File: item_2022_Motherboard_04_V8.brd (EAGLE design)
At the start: 160 x 100 mm, 130 parts, among them IC1 MCP602SN, IC2 LD117AS33TR, IC3 MCP1525TO, IC4 MCP6S26, IC5 MCP6004SO, IC6 MCP6004SO, IC7 MCP3204SL, IC8 LM336LP, IC9 MCP6004SO, U1 ESP32-DEVKITC-32D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

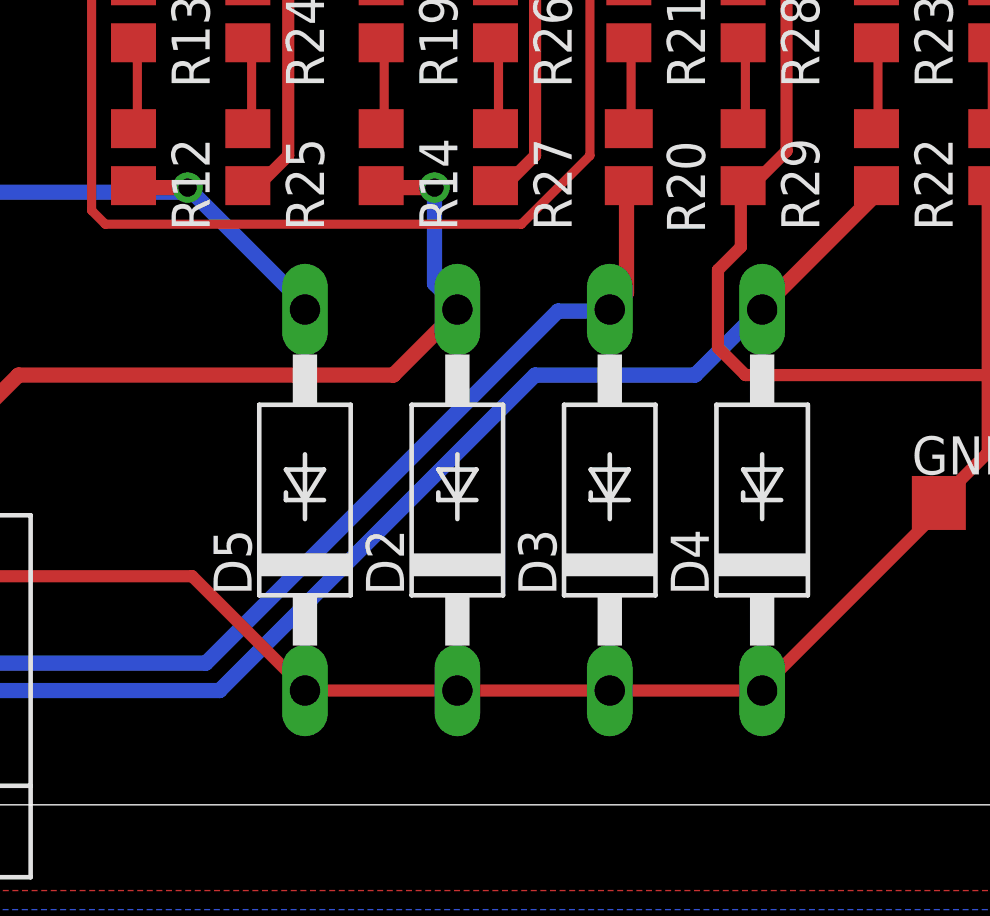
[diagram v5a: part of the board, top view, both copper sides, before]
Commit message: spostati BZW su Frontend da motherboard
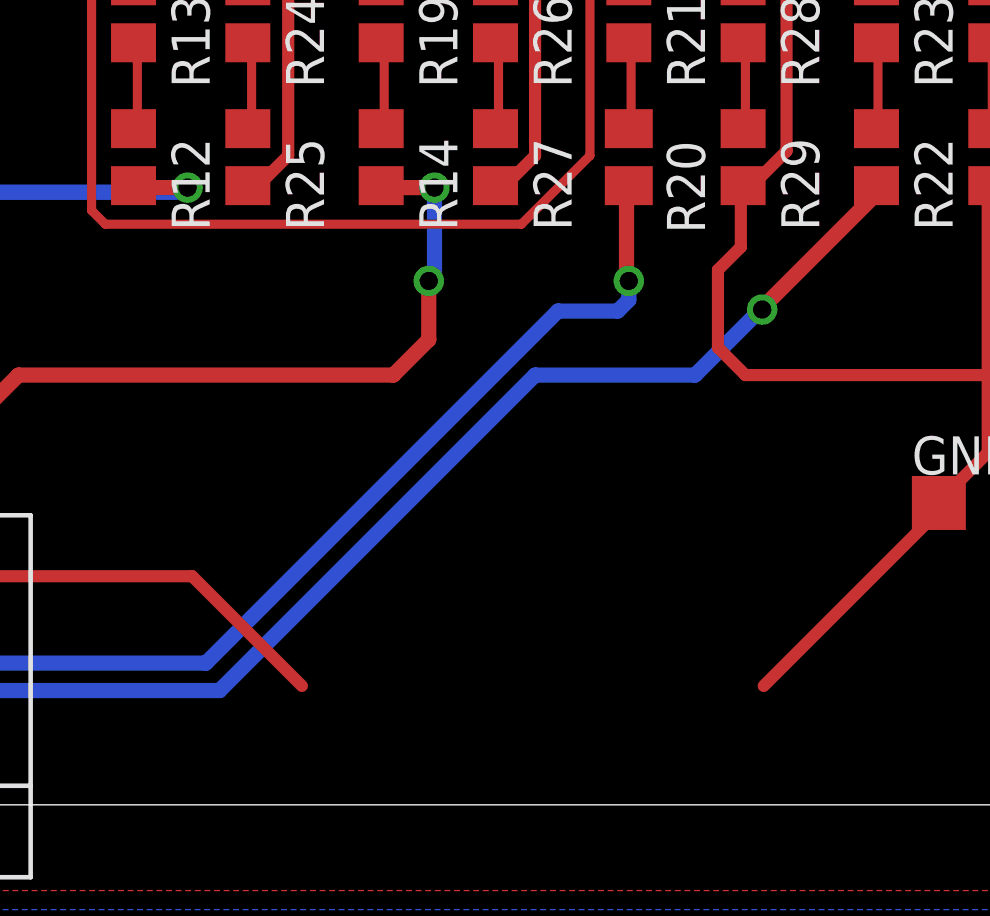
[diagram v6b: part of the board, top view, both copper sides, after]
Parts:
- removed D2, D3, D4, D5: BZW06-10B, diode_LargePads:F126Z12
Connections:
- net GND: no longer D2.C, D3.C, D4.C, D5.C
- net SPEED1+: no longer D3.A
- net SPEED2+: no longer D4.A
- net TORQUE1+: no longer D5.A
- net TORQUE2+: no longer D2.A
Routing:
- net GND: track 943.0 -> 927.4 mm
- net TORQUE1+: track 95.4 -> 89.6 mm
- net TORQUE2+: track 107.3 -> 106.9 mm, vias 1 -> 2
- net SPEED1+: track 111.4 -> 111.7 mm, vias 0 -> 1
- net SPEED2+: vias 0 -> 1
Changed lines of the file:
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@@
 <setting verticaltext="up"/>
 </settings>
-<grid distance="0.0125" unitdist="inch" unit="mm" style="lines" multiple="2" display="yes" altdistance="0.025" altunitdist="inch" altunit="inch"/>
+<grid distance="0.0125" unitdist="inch" unit="mil" style="lines" multiple="2" display="yes" altdistance="0.025" altunitdist="inch" altunit="inch"/>
 <layers>
 <layer number="1" name="Top" color="4" fill="1" visible="yes" active="yes"/>
@@
 <attribute name="VALUE" x="151.765" y="56.515" size="1.27" layer="27" rot="R270"/>
 </element>
-<element name="D2" library="diode_LargePads" package="F126Z12" value="BZW06-10B" x="133.35" y="10.16" smashed="yes" rot="R90">
-<attribute name="NAME" x="131.572" y="6.985" size="1.27" layer="25" ratio="10" rot="R90"/>
-<attribute name="POPULARITY" value="0" x="441.95" y="10.16" size="1.778" layer="27" rot="R90" display="off"/>
-<attribute name="VALUE" x="136.398" y="6.985" size="1.27" layer="27" ratio="10" rot="R90"/>
-</element>
-<element name="D3" library="diode_LargePads" package="F126Z12" value="BZW06-10B" x="138.43" y="10.16" smashed="yes" rot="R90">
-<attribute name="NAME" x="136.652" y="6.985" size="1.27" layer="25" ratio="10" rot="R90"/>
-<attribute name="POPULARITY" value="0" x="462.33" y="-17.84" size="1.778" layer="27" rot="R90" display="off"/>
-<attribute name="VALUE" x="141.478" y="6.985" size="1.27" layer="27" ratio="10" rot="R90"/>
-</element>
-<element name="D4" library="diode_LargePads" package="F126Z12" value="BZW06-10B" x="143.51" y="10.16" smashed="yes" rot="R90">
-<attribute name="NAME" x="141.732" y="6.985" size="1.27" layer="25" ratio="10" rot="R90"/>
-<attribute name="POPULARITY" value="0" x="467.41" y="10.16" size="1.778" layer="27" rot="R90" display="off"/>
-<attribute name="VALUE" x="146.558" y="6.985" size="1.27" layer="27" ratio="10" rot="R90"/>
-</element>
-<element name="D5" library="diode_LargePads" package="F126Z12" value="BZW06-10B" x="128.27" y="10.16" smashed="yes" rot="R90">
-<attribute name="NAME" x="126.492" y="6.985" size="1.27" layer="25" ratio="10" rot="R90"/>
-<attribute name="POPULARITY" value="0" x="467.47" y="-17.84" size="1.778" layer="27" rot="R90" display="off"/>
-<attribute name="VALUE" x="131.318" y="6.985" size="1.27" layer="27" ratio="10" rot="R90"/>
-</element>
 <element name="IC7" library="MCP3204_MCP3208" package="SO14" value="MCP3204SL" x="151.765" y="67.31" smashed="yes">
 <attribute name="NAME" x="146.939" y="65.405" size="1.27" layer="25" ratio="10" rot="R90"/>
@@
 <contactref element="R11" pad="1"/>
 <contactref element="C15" pad="2"/>
-<contactref element="D4" pad="C"/>
-<contactref element="D3" pad="C"/>
-<contactref element="D2" pad="C"/>
-<contactref element="D5" pad="C"/>
 <contactref element="R25" pad="2"/>
 <contactref element="C16" pad="2"/>
@@
 <wire x1="79.0956" y1="7.62" x2="79.0956" y2="21.6408" width="0.4064" layer="1"/>
 <wire x1="86.7156" y1="29.5656" x2="86.6775" y2="29.7975" width="0.4064" layer="1"/>
-<wire x1="143.51" y1="3.81" x2="138.43" y2="3.81" width="0.4064" layer="1"/>
-<wire x1="133.35" y1="3.81" x2="128.27" y2="3.81" width="0.4064" layer="1"/>
 <wire x1="124.5108" y1="7.62" x2="115.57" y2="7.62" width="0.4064" layer="1"/>
 <wire x1="128.1684" y1="3.9624" x2="124.5108" y2="7.62" width="0.4064" layer="1"/>
-<wire x1="128.1684" y1="3.9624" x2="128.27" y2="3.81" width="0.4064" layer="1"/>
-<wire x1="133.35" y1="3.81" x2="138.43" y2="3.81" width="0.4064" layer="1"/>
 <wire x1="143.256" y1="20.7264" x2="142.9512" y2="20.7264" width="0.4064" layer="1"/>
 <wire x1="144.3228" y1="21.7932" x2="143.256" y2="20.7264" width="0.4064" layer="1"/>
@@
 <wire x1="142.7988" y1="20.574" x2="142.875" y2="20.64" width="0.4064" layer="1"/>
 <wire x1="149.5044" y1="9.906" x2="143.5608" y2="3.9624" width="0.4064" layer="1"/>
-<wire x1="143.5608" y1="3.9624" x2="143.51" y2="3.81" width="0.4064" layer="1"/>
 <wire x1="149.5044" y1="9.906" x2="149.4" y2="10.0625" width="0.4064" layer="1"/>
 <wire x1="101.9556" y1="7.62" x2="100.33" y2="7.62" width="0.4064" layer="16"/>
@@
 <contactref element="PL1" pad="6"/>
 <contactref element="R12" pad="2"/>
-<contactref element="D5" pad="A"/>
 <wire x1="124.3584" y1="20.574" x2="122.682" y2="20.574" width="0.508" layer="1"/>
-<wire x1="128.3208" y1="16.6116" x2="124.3584" y2="20.574" width="0.508" layer="16"/>
 <wire x1="122.682" y1="20.574" x2="122.555" y2="20.64" width="0.508" layer="1"/>
-<wire x1="128.3208" y1="16.6116" x2="128.27" y2="16.51" width="0.508" layer="16"/>
 <wire x1="43.7388" y1="8.8392" x2="43.2816" y2="8.8392" width="0.508" layer="16"/>
 <wire x1="45.8724" y1="6.7056" x2="43.7388" y2="8.8392" width="0.508" layer="16"/>
@@
 <contactref element="PL1" pad="8"/>
 <contactref element="R14" pad="2"/>
-<contactref element="D2" pad="A"/>
 <wire x1="132.588" y1="20.574" x2="130.9116" y2="20.574" width="0.508" layer="1"/>
-<wire x1="132.588" y1="17.3736" x2="132.588" y2="20.574" width="0.508" layer="16"/>
-<wire x1="133.35" y1="16.6116" x2="132.588" y2="17.3736" width="0.508" layer="16"/>
+<wire x1="132.588" y1="17.3736" x2="132.588" y2="17.4625" width="0.508" layer="16"/>
+<wire x1="132.588" y1="17.4625" x2="132.588" y2="20.574" width="0.508" layer="16"/>
 <wire x1="130.9116" y1="20.574" x2="130.81" y2="20.64" width="0.508" layer="1"/>
-<wire x1="133.35" y1="16.6116" x2="133.35" y2="16.51" width="0.508" layer="16"/>
 <wire x1="41.148" y1="8.8392" x2="40.6908" y2="8.8392" width="0.508" layer="1"/>
 <wire x1="46.0248" y1="3.9624" x2="41.148" y2="8.8392" width="0.508" layer="1"/>
@@
 <wire x1="118.7196" y1="14.3256" x2="113.8428" y2="9.4488" width="0.508" layer="1"/>
 <wire x1="131.2164" y1="14.3256" x2="118.7196" y2="14.3256" width="0.508" layer="1"/>
-<wire x1="133.35" y1="16.4592" x2="131.2164" y2="14.3256" width="0.508" layer="1"/>
 <wire x1="40.6908" y1="8.8392" x2="40.64" y2="8.89" width="0.508" layer="1"/>
-<wire x1="133.35" y1="16.4592" x2="133.35" y2="16.51" width="0.508" layer="1"/>
 <via x="132.588" y="20.574" extent="1-16" drill="0.6096"/>
+<via x="132.3975" y="17.4625" extent="1-16" drill="0.6096"/>
+<wire x1="132.3975" y1="17.4625" x2="132.588" y2="17.4625" width="0.508" layer="16"/>
+<wire x1="132.3975" y1="17.4625" x2="132.3975" y2="15.5067" width="0.508" layer="1"/>
+<wire x1="132.3975" y1="15.5067" x2="131.2164" y2="14.3256" width="0.508" layer="1"/>
 </signal>
 <signal name="SPEED1+" class="3">
 <contactref element="PL1" pad="10"/>
 <contactref element="R20" pad="2"/>
-<contactref element="D3" pad="A"/>
-<wire x1="138.9888" y1="17.0688" x2="138.9888" y2="20.574" width="0.508" layer="1"/>
-<wire x1="138.43" y1="16.51" x2="138.9888" y2="17.0688" width="0.508" layer="1"/>
+<wire x1="138.9888" y1="17.3863" x2="138.9888" y2="17.4625" width="0.508" layer="1"/>
+<wire x1="138.9888" y1="17.4625" x2="138.9888" y2="20.574" width="0.508" layer="1"/>
 <wire x1="138.9888" y1="20.574" x2="139.065" y2="20.64" width="0.508" layer="1"/>
 <wire x1="38.7096" y1="8.8392" x2="38.1" y2="8.8392" width="0.508" layer="16"/>
@@
 <wire x1="124.968" y1="4.7244" x2="42.8244" y2="4.7244" width="0.508" layer="16"/>
 <wire x1="136.7028" y1="16.4592" x2="124.968" y2="4.7244" width="0.508" layer="16"/>
-<wire x1="138.3792" y1="16.4592" x2="136.7028" y2="16.4592" width="0.508" layer="16"/>
+<wire x1="138.6967" y1="16.4592" x2="136.7028" y2="16.4592" width="0.508" layer="16"/>
 <wire x1="38.1" y1="8.8392" x2="38.1" y2="8.89" width="0.508" layer="16"/>
-<wire x1="138.3792" y1="16.4592" x2="138.43" y2="16.51" width="0.508" layer="16"/>
+<via x="139.065" y="17.4625" extent="1-16" drill="0.6096"/>
+<wire x1="138.6967" y1="16.4592" x2="139.065" y2="16.8275" width="0.508" layer="16"/>
+<wire x1="139.065" y1="16.8275" x2="139.065" y2="17.4625" width="0.508" layer="16"/>
+<wire x1="139.065" y1="17.4625" x2="138.9888" y2="17.4625" width="0.508" layer="1"/>
 </signal>
 <signal name="SPEED2+" class="3">
 <contactref element="PL1" pad="12"/>
 <contactref element="R22" pad="2"/>
-<contactref element="D4" pad="A"/>
 <wire x1="147.2184" y1="20.2692" x2="147.2184" y2="20.574" width="0.508" layer="1"/>
 <wire x1="143.5608" y1="16.6116" x2="147.2184" y2="20.2692" width="0.508" layer="1"/>
 <wire x1="147.2184" y1="20.574" x2="147.32" y2="20.64" width="0.508" layer="1"/>
-<wire x1="143.5608" y1="16.6116" x2="143.51" y2="16.51" width="0.508" layer="1"/>
 <wire x1="36.1188" y1="8.8392" x2="35.6616" y2="8.8392" width="0.508" layer="16"/>
 <wire x1="41.148" y1="3.81" x2="36.1188" y2="8.8392" width="0.508" layer="16"/>
@@
 <wire x1="143.4084" y1="16.4592" x2="141.2748" y2="14.3256" width="0.508" layer="16"/>
 <wire x1="35.6616" y1="8.8392" x2="35.56" y2="8.89" width="0.508" layer="16"/>
-<wire x1="143.4084" y1="16.4592" x2="143.51" y2="16.51" width="0.508" layer="16"/>
+<via x="143.51" y="16.51" extent="1-16" drill="0.6096"/>
+<wire x1="143.4084" y1="16.4592" x2="143.4592" y2="16.4592" width="0.508" layer="16"/>
+<wire x1="143.4592" y1="16.4592" x2="143.51" y2="16.51" width="0.508" layer="16"/>
+<wire x1="143.5608" y1="16.6116" x2="143.5608" y2="16.5608" width="0.508" layer="1"/>
+<wire x1="143.5608" y1="16.5608" x2="143.51" y2="16.51" width="0.508" layer="1"/>
 </signal>
 <signal name="EXT_+5V" class="1">

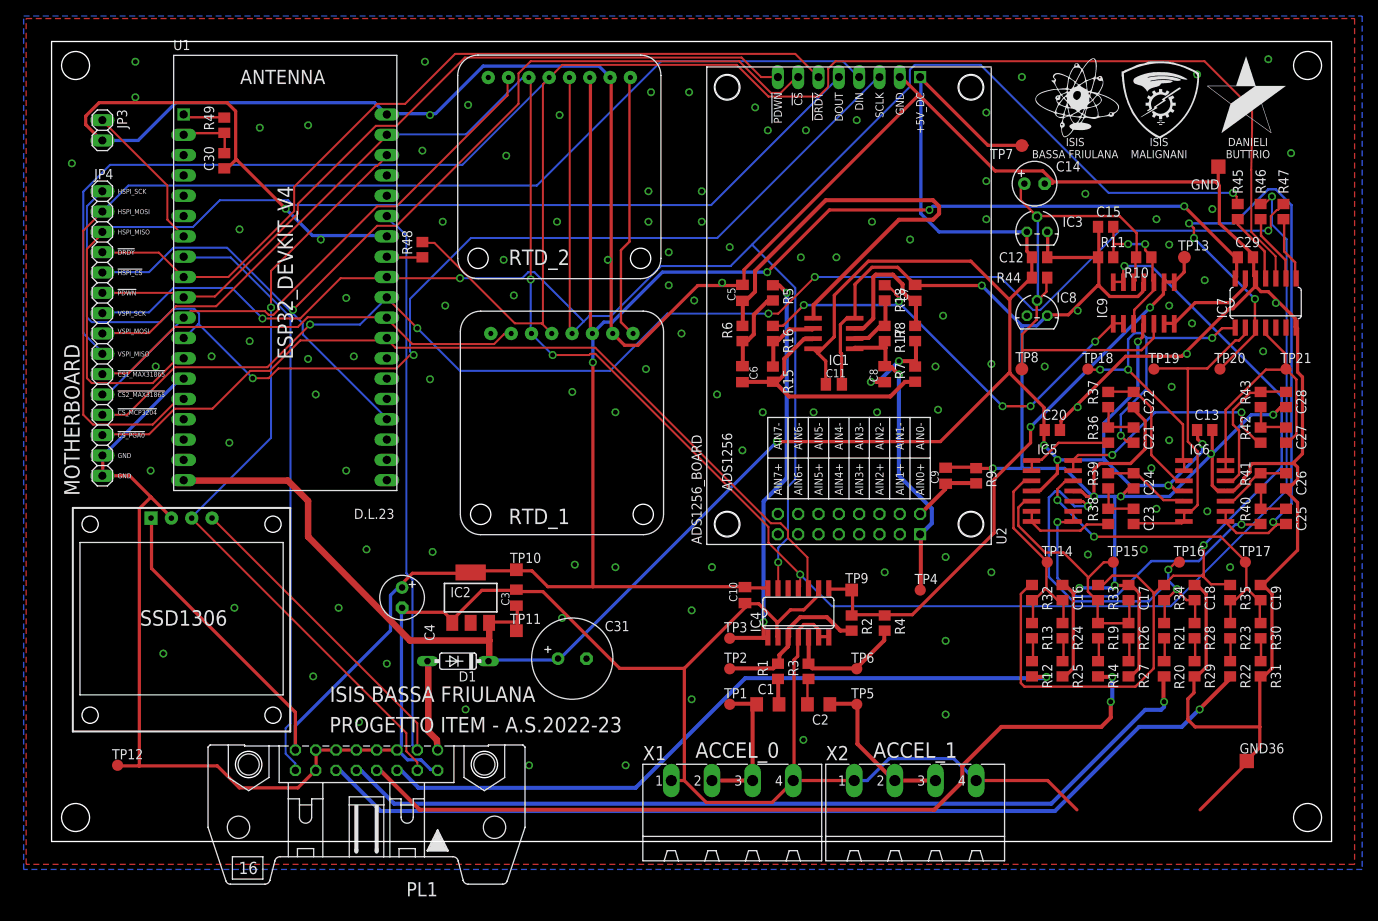
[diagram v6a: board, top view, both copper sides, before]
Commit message: MCP6S28 DIL
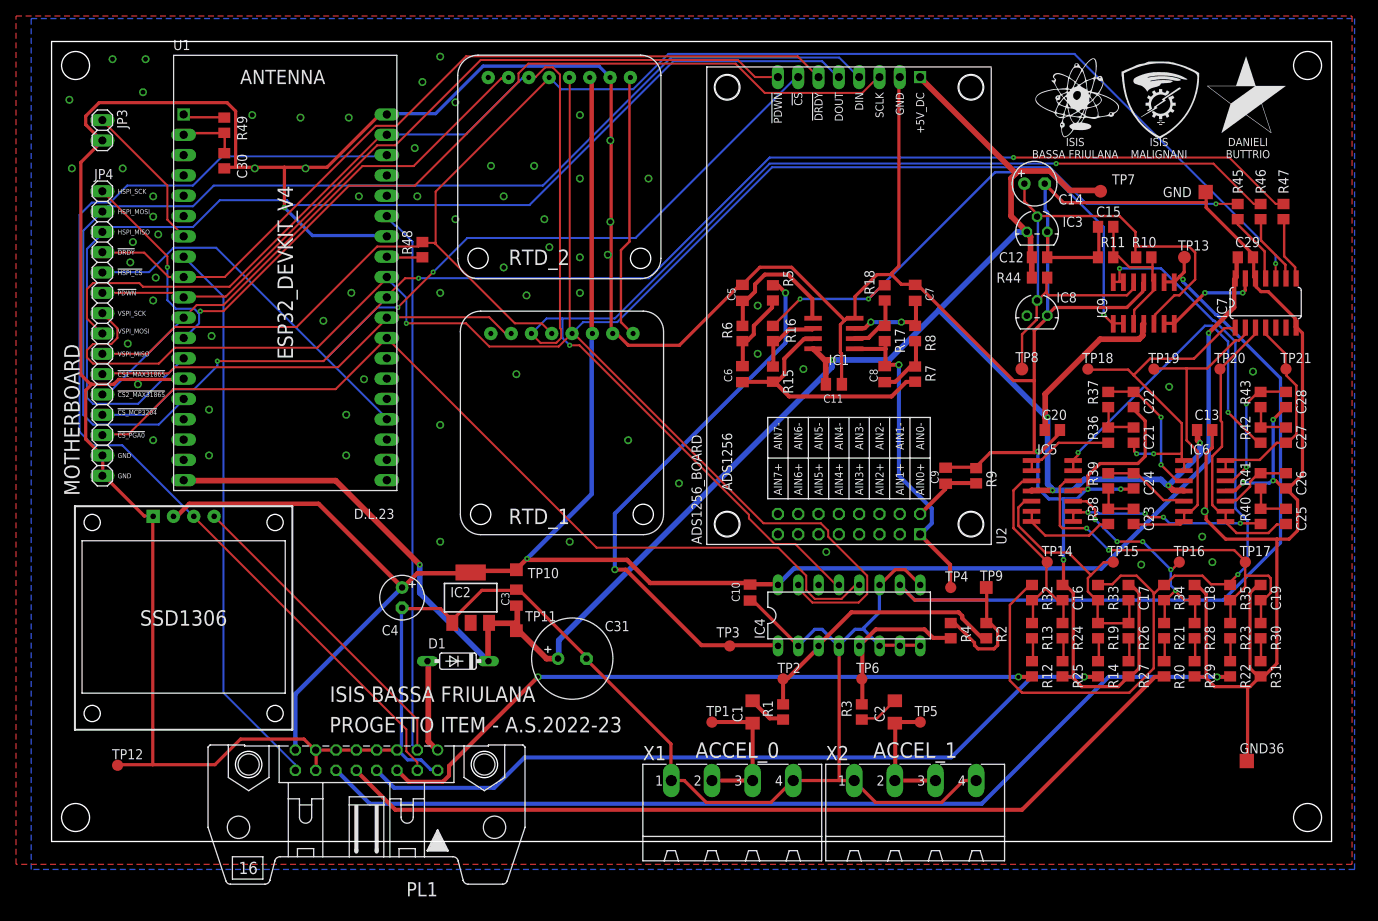
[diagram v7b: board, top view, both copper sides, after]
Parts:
- IC4: value MCP6S26 -> MCP6S28DIL; device microchip_opamp:SO14 -> microchip_opamp:DIL16
- moved R2 16.9 mm to (116.8, 26.4)
- moved TP9 16.8 mm to (116.8, 31.8)
- moved TP7 11.4 mm to (131.1, 81.3)
- moved C2 9.57 mm to (105.4, 16.2), turned to 90 degrees
- moved R3 8.38 mm to (101.3, 16.2)
- moved R4 8.31 mm to (112.4, 26.4)
- moved TP5 8.24 mm to (108.6, 14.9)
- moved TP2 6.79 mm to (91.4, 20.3)
- moved IC4 6.36 mm to (99.7, 28.3)
- moved R1 5.12 mm to (91.4, 16.2)
- moved TP4 3.82 mm to (112.4, 31.8)
- moved GND 3.55 mm to (144.3, 81.2)
- moved TP1 3.14 mm to (82.5, 14.9)
- moved C1 2.13 mm to (87.6, 16.2), turned to 90 degrees
- moved TP6 1.42 mm to (101.3, 20.3)
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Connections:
- net !CS_PGA0!: now also IC4.12; no longer IC4.10
- net +3V3: now also IC4.16, U3.2; no longer IC4.14, U3.VCC
- net ADC_HALF_VREF_A: now also IC4.10; no longer IC4.8
- net GND: now also IC4.11, IC4.8, U3.1; no longer U3.GND
- net I2C_SCL: now also U3.3; no longer U3.SCL
- net I2C_SDA: now also U3.4; no longer U3.SDA
- net VSPI_MOSI: now also IC4.13; no longer IC4.11
- net VSPI_SCK: now also IC4.15; no longer IC4.13
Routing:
- net VSPI_MISO: track 255.8 -> 200.0 mm, vias 0 -> 1
- net A_SPEED1: track 89.9 -> 36.6 mm, vias 4 -> 0
- net ADC_HALF_VREF_A: track 73.5 -> 122.2 mm, vias 2 -> 1
- net GND: track 927.4 -> 885.4 mm, vias 122 -> 76
- net N$10: track 58.0 -> 17.7 mm
- net +5V: track 313.8 -> 278.5 mm
- net I2C_SCL: track 98.8 -> 130.7 mm, vias 1 -> 0
- net N$26: track 50.9 -> 31.6 mm, vias 3 -> 5
- net N$5: track 51.2 -> 69.8 mm
- net HSPI_SCK: track 144.1 -> 126.6 mm
- net VSPI_SCK: track 252.6 -> 269.3 mm, vias 4 -> 2
- net N$30: track 40.4 -> 25.4 mm, vias 2 -> 4
- net N$31: track 29.8 -> 43.1 mm
- net N$4: track 20.4 -> 33.7 mm
- net VSPI_MOSI: track 255.7 -> 267.4 mm, vias 4 -> 2
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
